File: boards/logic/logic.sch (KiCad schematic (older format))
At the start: 38 parts

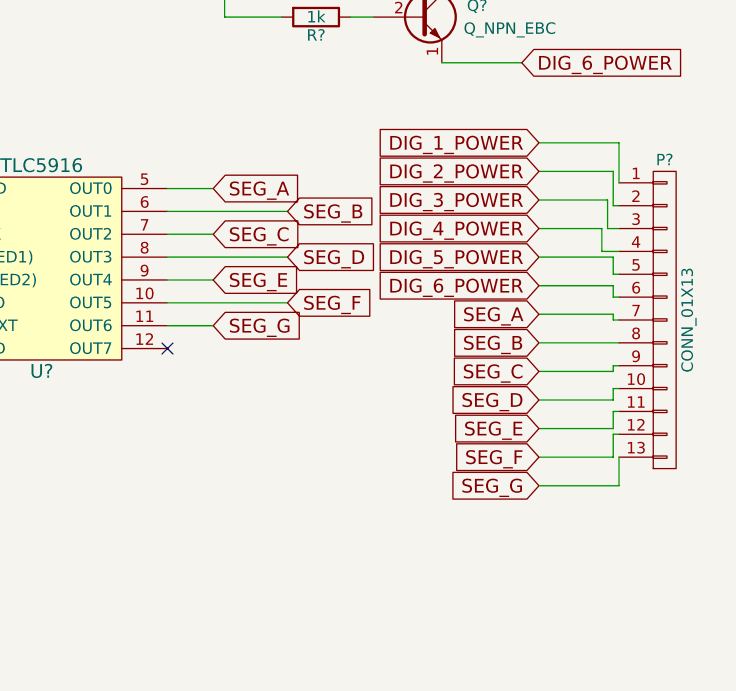
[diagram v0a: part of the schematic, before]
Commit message: Use the 8th output of the TLC5916 for the decimal point.
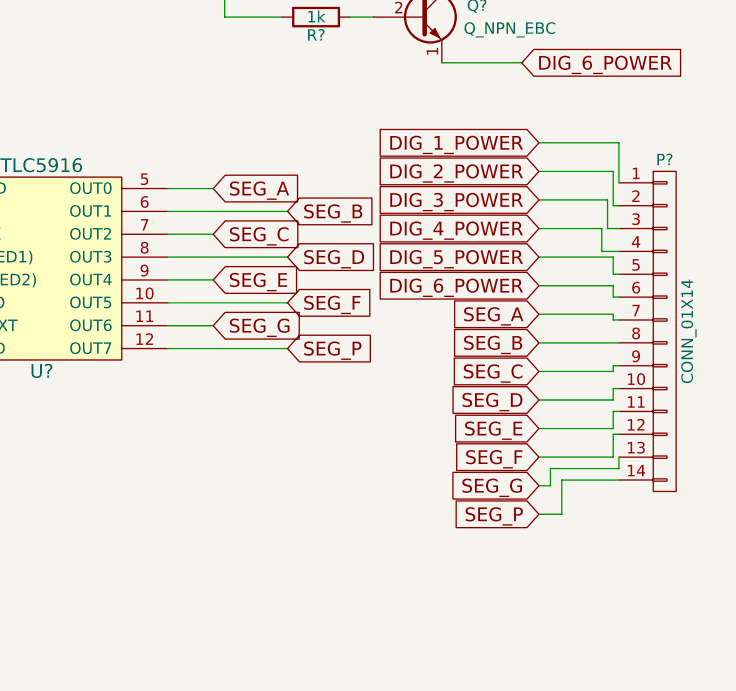
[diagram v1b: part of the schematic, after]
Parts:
- removed P?: CONN_01X13, symbol CONN_01X13
- added P?: CONN_01X14, symbol CONN_01X14
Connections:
- net DIG_1_POWER: now also P?.1 (P1)
- net DIG_2_POWER: now also P?.2 (P2)
- net DIG_3_POWER: now also P?.3 (P3)
- net DIG_4_POWER: now also P?.4 (P4)
- net DIG_5_POWER: now also P?.5 (P5)
- net DIG_6_POWER: now also P?.6 (P6)
- net SEG_A: now also P?.7 (P7)
- net SEG_B: now also P?.8 (P8)
- net SEG_C: now also P?.9 (P9)
- net SEG_D: now also P?.10 (P10)
- net SEG_E: now also P?.11 (P11)
- net SEG_F: now also P?.12 (P12)
- net SEG_G: now also P?.13 (P13)
- net SEG_P: now reaches U?.12 (OUT7)
- net SEG_P: now also P?.14 (P14)
- no-connect marks 12 -> 11
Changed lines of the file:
@@
 Text GLabel 9050 5550 2    60   Input ~ 0
 SEG_G
-NoConn ~ 8850 5650
 $Comp
 L C C?
@@
 	1    4375 1075
 	0    1    1    0
-$EndComp
-$Comp
-L CONN_01X13 P?
-U 1 1 57634E0A
-P 11025 5525
-F 0 "P?" H 11025 6225 50  0000 C CNN
-F 1 "CONN_01X13" V 11125 5525 50  0000 C CNN
-F 2 "" H 11025 5525 50  0000 C CNN
-F 3 "" H 11025 5525 50  0000 C CNN
-	1    11025 5525
-	1    0    0    -1
 $EndComp
 Text GLabel 10475 4750 0    60   Input ~ 0
@@
 	10825 4750 10825 4925
 Wire Wire Line
-	10475 6250 10825 6250
-Wire Wire Line
-	10825 6250 10825 6125
-Wire Wire Line
 	10475 6125 10800 6125
 Wire Wire Line
@@
 Wire Wire Line
 	3300 4425 3300 4525
+$Comp
+L CONN_01X14 P?
+U 1 1 57D59A74
+P 11025 5575
+F 0 "P?" H 11025 6325 50  0000 C CNN
+F 1 "CONN_01X14" V 11125 5575 50  0000 C CNN
+F 2 "" H 11025 5575 50  0000 C CNN
+F 3 "" H 11025 5575 50  0000 C CNN
+	1    11025 5575
+	1    0    0    -1
+$EndComp
+Wire Wire Line
+	10825 6125 10825 6175
+Wire Wire Line
+	10825 6175 10525 6175
+Wire Wire Line
+	10525 6175 10525 6250
+Wire Wire Line
+	10525 6250 10475 6250
+Text GLabel 9375 5650 2    60   Input ~ 0
+SEG_P
+Wire Wire Line
+	8850 5650 9375 5650
+Text GLabel 10475 6375 0    60   Input ~ 0
+SEG_P
+Wire Wire Line
+	10475 6375 10575 6375
+Wire Wire Line
+	10575 6375 10575 6225
+Wire Wire Line
+	10575 6225 10825 6225
 $EndSCHEMATC

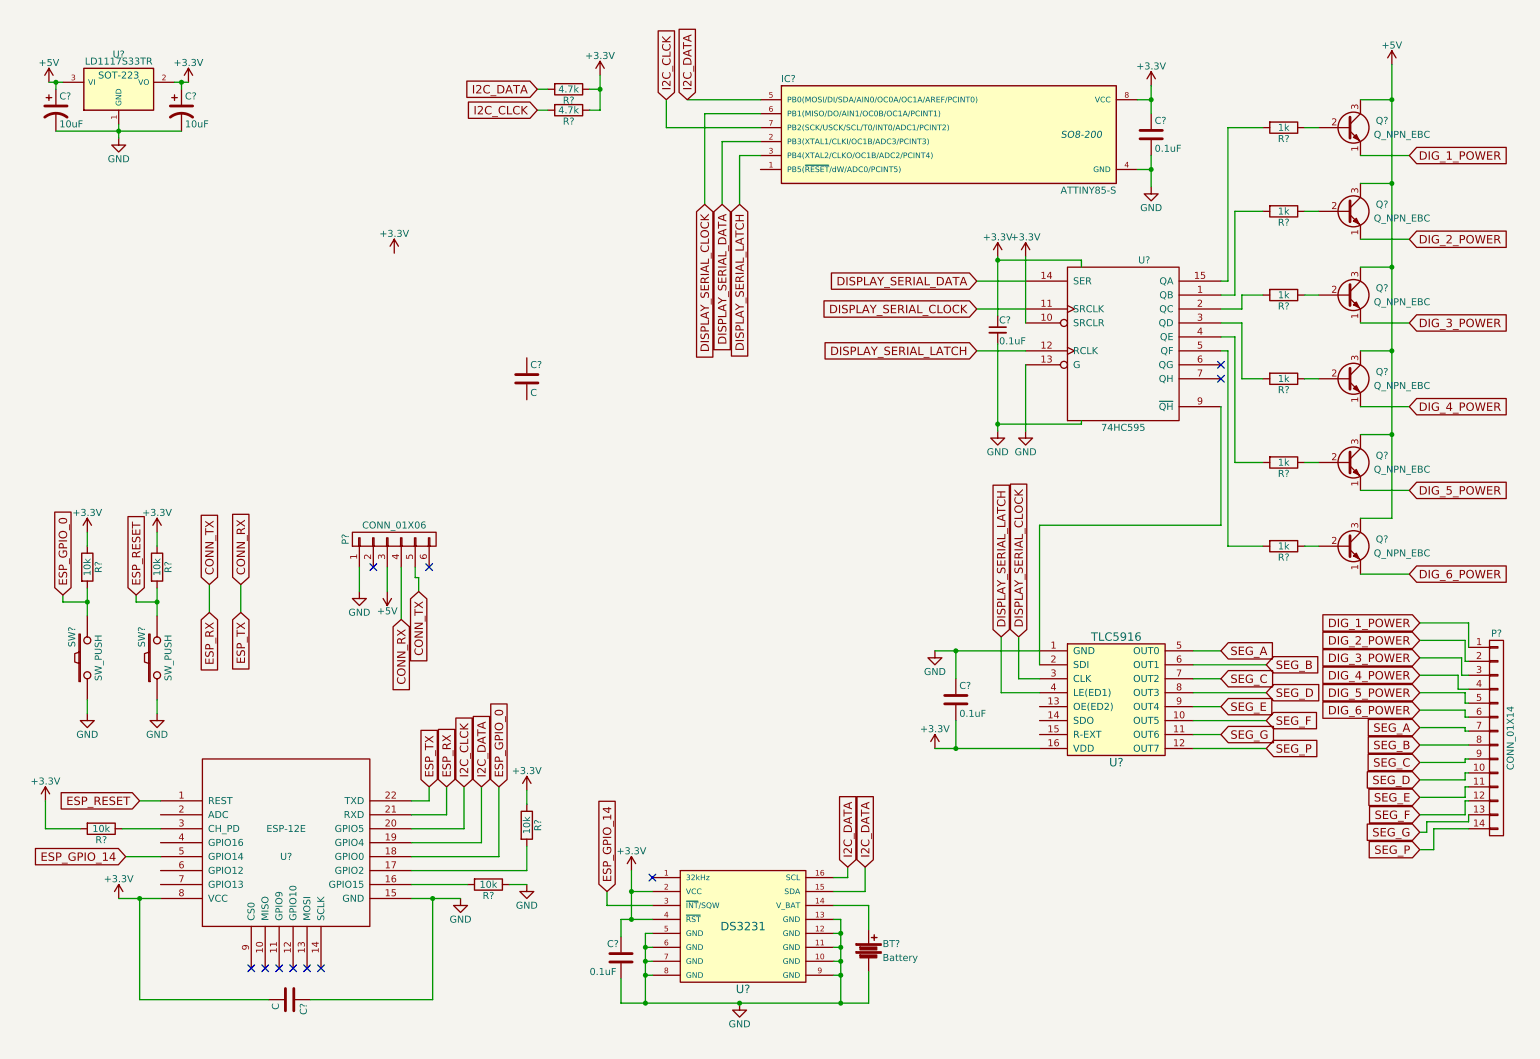
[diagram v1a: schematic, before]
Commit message: Add a 5V input to the board, and re-layout the schematic for easier reading.
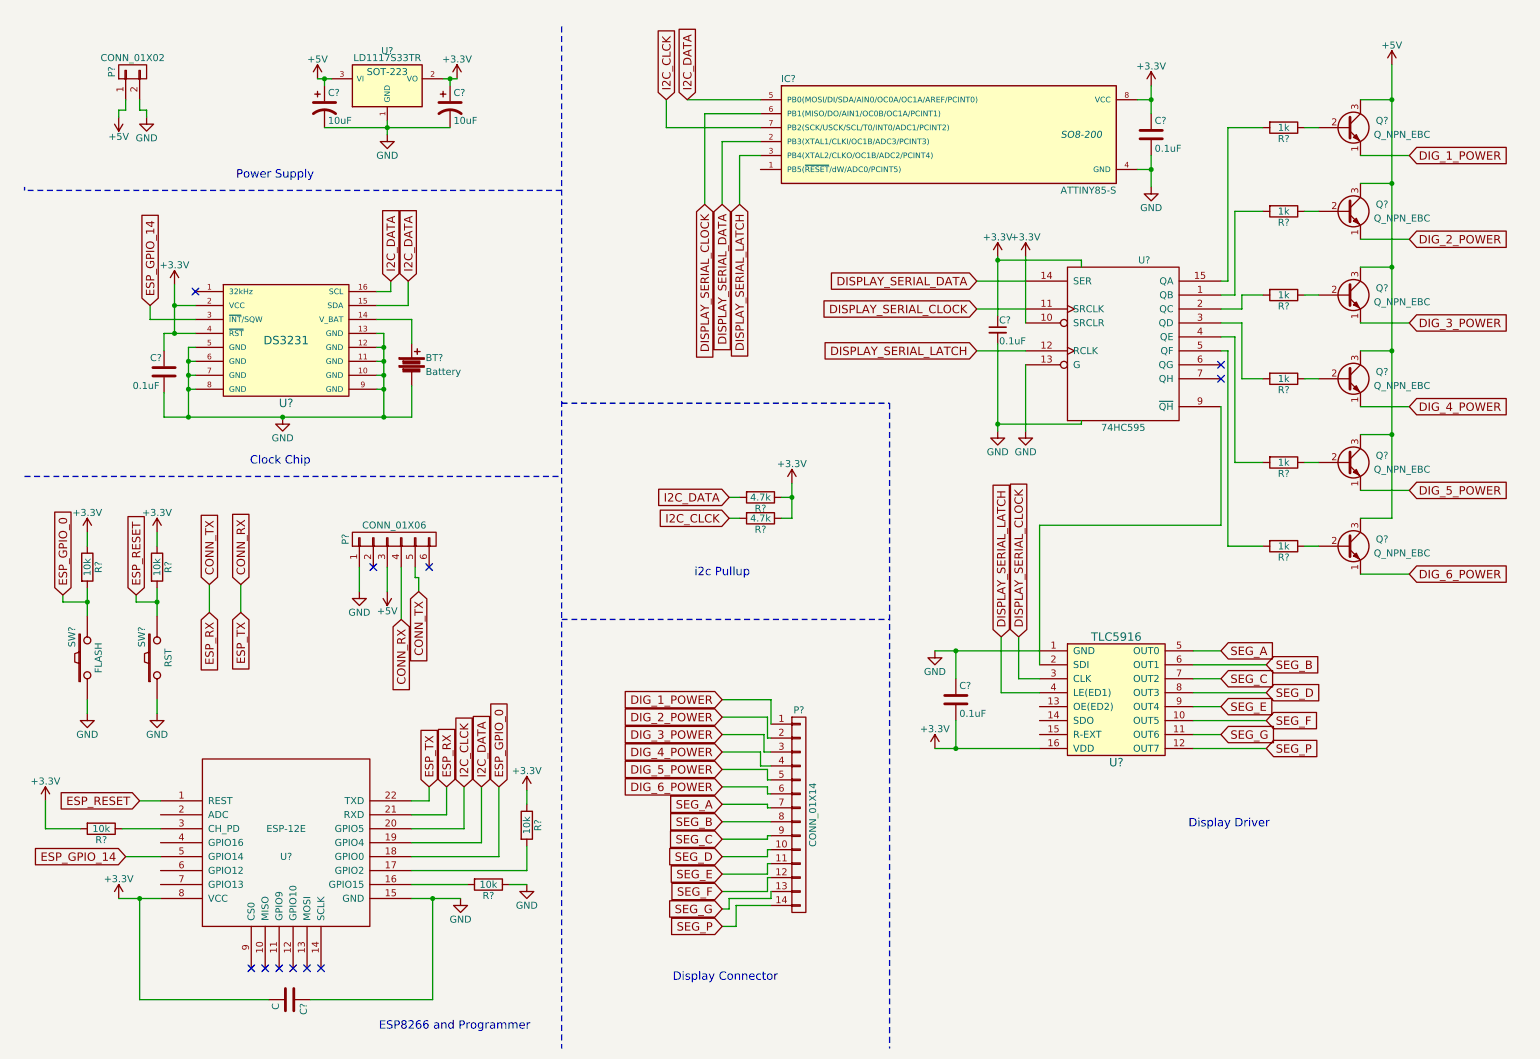
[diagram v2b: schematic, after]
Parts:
- removed C?: C, symbol C
- added P?: CONN_01X02, symbol CONN_01X02
- SW?: value SW_PUSH -> FLASH
- SW?: value SW_PUSH -> RST
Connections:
- net +5V: now also P?.1 (P1)
- net GND: now also P?.2 (P2)
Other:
- note added: "Clock Chip"
- note added: "Display Connector"
- note added: "Display Driver"
- note added: "ESP8266 and Programmer"
- note added: "Power Supply"
- note added: "i2c Pullup"
- moved on the sheet: BT?, C?, P?, R?, U?

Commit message: Add a missing pullup to the DS3231 interrupt pin, and add some NC symbols.
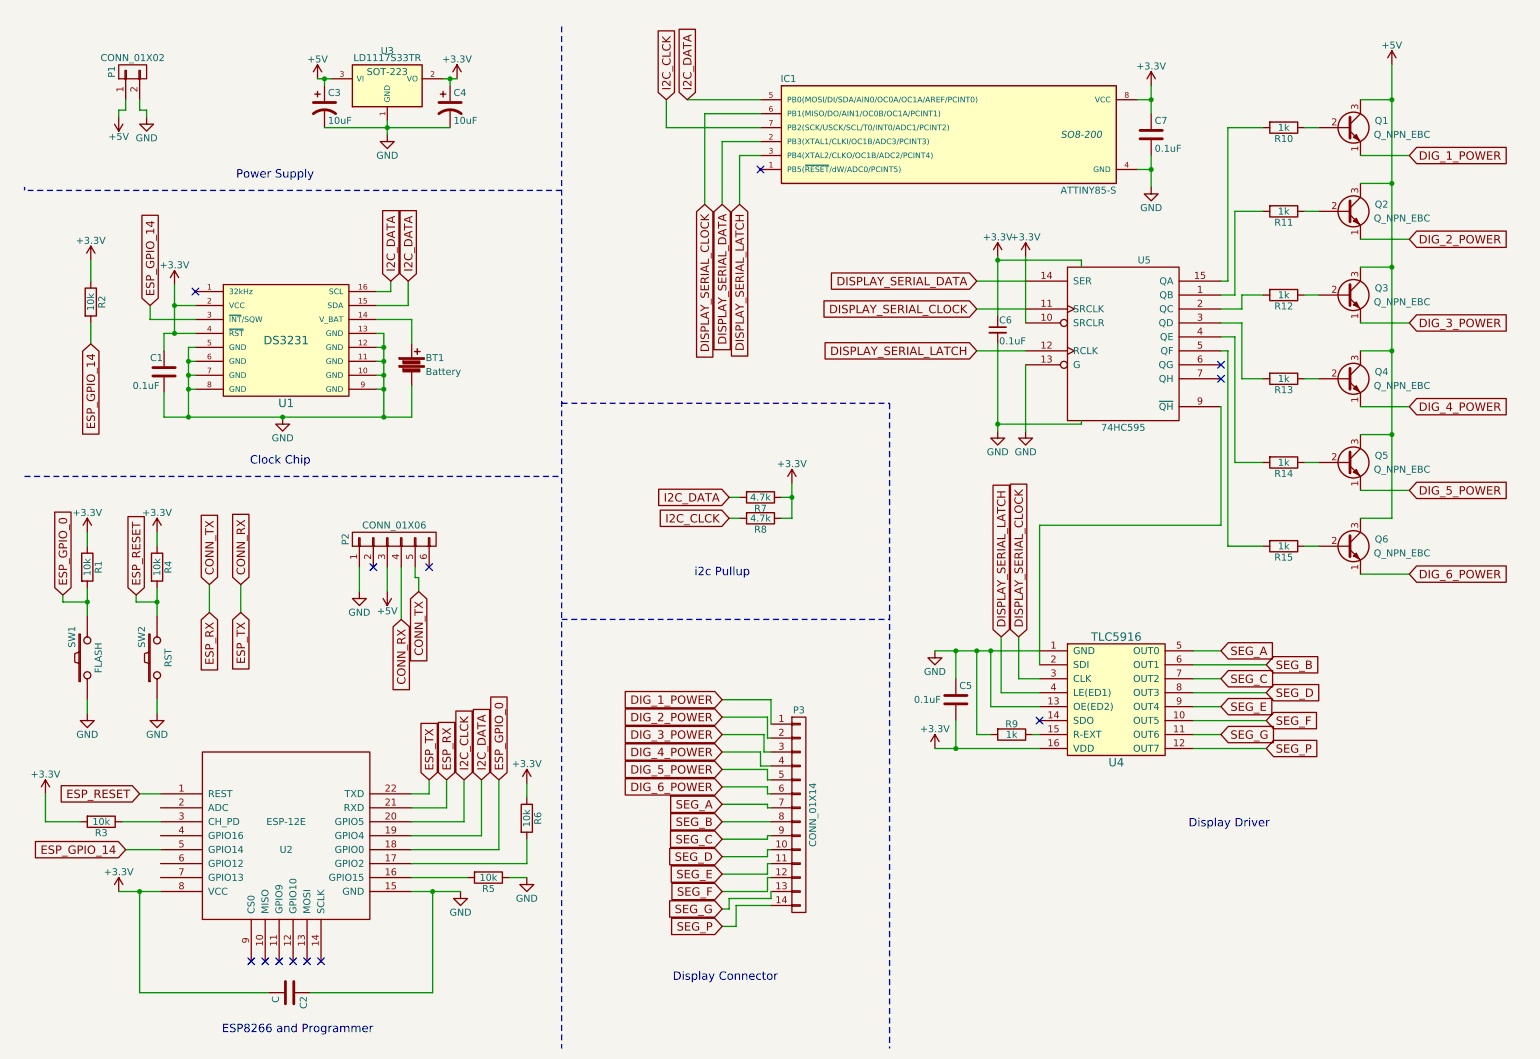
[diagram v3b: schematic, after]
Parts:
- added R2: 10k, symbol R
- added R9: 1k, symbol R
- gave numbers to parts that had none: 38
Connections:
- net +3V3: now also R2.1
- net ESP_GPIO_14: now also R2.2
- net GND: now also U4.13 (OE(ED2)), R9.2
- net at U4.15 (R-EXT): now also R9.1
- no-connect marks 11 -> 13
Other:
- moved on the sheet: C2, R3, R5, R6, U2
